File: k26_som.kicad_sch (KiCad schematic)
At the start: 48 parts, among them J6 22-23-2021, M1 XILINX-KRIA-K26, Q6 PJA3441, Q7 DTC014TEBTL

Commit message: Add decoupling to cammera and DP connector, schematic cleanup
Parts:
- added R?: R_0R_0402, antmicro-footprints:0402-res, symbol antmicroResistors0402:R_0R_0402
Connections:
- net GND: now also R?.1
- net VCC_BATT: now also R?.2
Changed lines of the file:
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@@
   (junction (at 85.09 55.88) (diameter 0) (color 0 0 0 0)
   )
-  (junction (at 373.38 177.8) (diameter 0) (color 0 0 0 0)
-  )
-  (junction (at 373.38 175.26) (diameter 0) (color 0 0 0 0)
-  )
   (junction (at 302.006 226.568) (diameter 0) (color 0 0 0 0)
   )
@@
     (stroke (width 0) (type default) (color 0 0 0 0))
   )
+  (wire (pts (xy 19.685 25.4) (xy 19.685 26.67))
+    (stroke (width 0) (type default) (color 0 0 0 0))
+  )
   (bus (pts (xy 196.85 129.54) (xy 196.85 134.62))
     (stroke (width 0) (type default) (color 0 0 0 0))
@@
     (stroke (width 0) (type default) (color 0 0 0 0))
   )
+  (wire (pts (xy 373.38 177.8) (xy 404.495 177.8))
+    (stroke (width 0) (type default) (color 0 0 0 0))
+  )
   (wire (pts (xy 277.368 223.52) (xy 277.368 226.06))
     (stroke (width 0) (type default) (color 0 0 0 0))
@@
     (stroke (width 0) (type default) (color 0 0 0 0))
   )
-  (wire (pts (xy 373.38 177.8) (xy 373.126 177.8))
-    (stroke (width 0) (type default) (color 0 0 0 0))
-  )
   (polyline (pts (xy 344.805 246.38) (xy 344.805 181.61))
     (stroke (width 0) (type default) (color 0 0 0 0))
@@
     (stroke (width 0) (type default) (color 0 0 0 0))
   )
+  (wire (pts (xy 19.685 34.29) (xy 19.685 35.56))
+    (stroke (width 0) (type default) (color 0 0 0 0))
+  )
   (wire (pts (xy 147.32 83.82) (xy 130.81 83.82))
     (stroke (width 0) (type default) (color 0 0 0 0))
@@
     (stroke (width 0) (type default) (color 0 0 0 0))
   )
-  (wire (pts (xy 50.8 25.4) (xy 25.4 25.4))
+  (wire (pts (xy 19.685 25.4) (xy 50.8 25.4))
     (stroke (width 0) (type default) (color 0 0 0 0))
   )
@@
     (stroke (width 0) (type default) (color 0 0 0 0))
   )
+  (wire (pts (xy 373.38 175.26) (xy 404.495 175.26))
+    (stroke (width 0) (type default) (color 0 0 0 0))
+  )
   (wire (pts (xy 81.28 66.04) (xy 96.774 66.04))
     (stroke (width 0) (type default) (color 0 0 0 0))
@@
     (stroke (width 0) (type default) (color 0 0 0 0))
   )
-  (wire (pts (xy 373.38 177.8) (xy 404.114 177.8))
-    (stroke (width 0) (type default) (color 0 0 0 0))
-  )
   (wire (pts (xy 133.35 265.684) (xy 157.48 265.684))
     (stroke (width 0) (type default) (color 0 0 0 0))
@@
     (stroke (width 0) (type default) (color 0 0 0 0))
   )
-  (wire (pts (xy 373.38 175.26) (xy 404.114 175.26))
-    (stroke (width 0) (type default) (color 0 0 0 0))
-  )
   (wire (pts (xy 246.38 86.36) (xy 224.282 86.36))
     (stroke (width 0) (type default) (color 0 0 0 0))
@@
     (stroke (width 0) (type default) (color 0 0 0 0))
   )
-  (wire (pts (xy 373.38 175.26) (xy 373.126 175.26))
-    (stroke (width 0) (type default) (color 0 0 0 0))
-  )
   (wire (pts (xy 317.5 33.02) (xy 342.9 33.02))
     (stroke (width 0) (type default) (color 0 0 0 0))
@@
     (effects (font (size 1.27 1.27)) (justify left bottom))
   )
-  (label "VCCO_HDC_1" (at 404.114 175.26 180)
+  (label "VCCO_HDC_1" (at 404.495 175.26 180)
     (effects (font (size 1.27 1.27)) (justify right bottom))
   )
@@
     (effects (font (size 1.27 1.27)) (justify left bottom))
   )
-  (label "VCCO_HDC_2" (at 404.114 177.8 180)
+  (label "VCCO_HDC_2" (at 404.495 177.8 180)
     (effects (font (size 1.27 1.27)) (justify right bottom))
   )
@@
     (pin "1")
   )
+  (symbol (lib_id "kria-k26-devboard:GND") (at 19.685 35.56 0) (unit 1)
+    (in_bom yes) (on_board yes)
+    (property "Reference" "#PWR?" (id 0) (at 19.685 41.91 0)
+      (effects (font (size 1.27 1.27)) hide)
+    )
+    (property "Value" "GND" (id 1) (at 19.812 39.9542 0))
+    (property "Footprint" "" (id 2) (at 19.685 35.56 0)
+      (effects (font (size 1.27 1.27)) hide)
+    )
+    (property "Datasheet" "" (id 3) (at 19.685 35.56 0)
+      (effects (font (size 1.27 1.27)) hide)
+    )
+    (pin "1")
+  )
   (symbol (lib_id "kria-k26-devboard:C_100n_0402") (at 258.445 272.415 0) (unit 1)
     (in_bom yes) (on_board yes)
@@
     (pin "1")
   )
+  (symbol (lib_id "antmicroResistors0402:R_0R_0402") (at 19.685 30.48 90) (unit 1)
+    (in_bom yes) (on_board yes) (fields_autoplaced)
+    (property "Reference" "R?" (id 0) (at 21.463 29.6454 90)
+      (effects (font (size 1.524 1.524)) (justify right))
+    )
+    (property "Value" "R_0R_0402" (id 1) (at 23.495 30.48 0)
+      (effects (font (size 1.524 1.524)) hide)
+    )
+    (property "Footprint" "antmicro-footprints:0402-res" (id 2) (at 14.605 25.4 0)
+      (effects (font (size 1.524 1.524)) (justify left) hide)
+    )
+    (property "Datasheet" "" (id 3) (at 19.685 30.48 0)
+      (effects (font (size 1.27 1.27)) hide)
+    )
+    (property "Manufacturer" "PANASONIC" (id 4) (at 9.525 25.4 0)
+      (effects (font (size 1.524 1.524)) (justify left) hide)
+    )
+    (property "MPN" "ERJ2GE0R00X" (id 5) (at 12.065 25.4 0)
+      (effects (font (size 1.524 1.524)) (justify left) hide)
+    )
+    (property "Val" "0R" (id 6) (at 21.463 32.4105 90)
+      (effects (font (size 1.27 1.27)) (justify right))
+    )
+    (pin "1")
+    (pin "2")
+  )
   (symbol (lib_id "kria-k26-devboard:TP_SMD_0_75MM") (at 386.715 206.375 90) (mirror x) (unit 1)

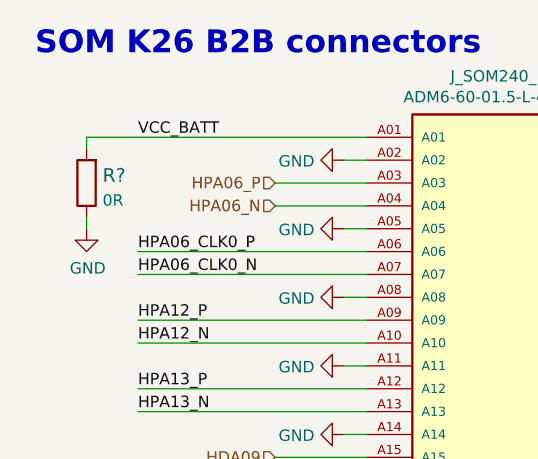
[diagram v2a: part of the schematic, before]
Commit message: Finish implementing review changes on schematic. Push to PCB
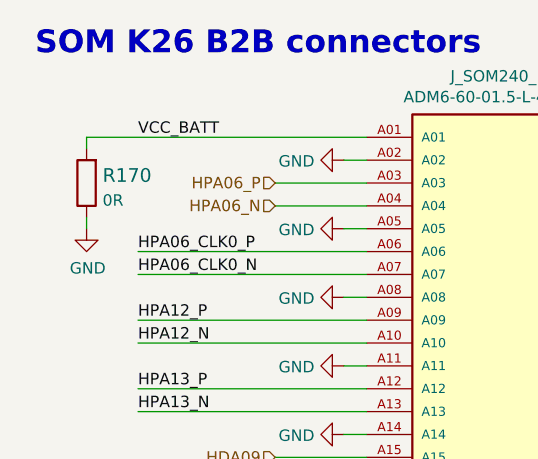
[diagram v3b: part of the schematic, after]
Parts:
- gave numbers to parts that had none: 1
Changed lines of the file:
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@@
   (title_block
     (title "Kria K26 Devboard")
-    (date "2023-02-15")
+    (date "2023-03-03")
     (rev "1.1.1")
     (company "Antmicro")
@@
   (symbol (lib_id "antmicroResistors0402:R_0R_0402") (at 19.685 30.48 90) (unit 1)
     (in_bom yes) (on_board yes) (fields_autoplaced)
-    (property "Reference" "R?" (id 0) (at 21.463 29.6454 90)
+    (property "Reference" "R170" (id 0) (at 21.463 29.6454 90)
       (effects (font (size 1.524 1.524)) (justify right))
     )

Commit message: Loclib of the project
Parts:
- R170: footprint antmicro-footprints:0402-res -> kria-k26-devboard-footprints:0402-res; symbol antmicroResistors0402:R_0R_0402 -> kria-k26-devboard:R_0R_0402

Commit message: Bom optimization
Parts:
- removed C126: C_1u_1210_100V, kria-k26-devboard-footprints:1210-cap, symbol kria-k26-devboard:C_1u_1210_100V
- added C126, C250, C251, C252, C253: C_100n_0402, kria-k26-devboard-footprints:0402-cap, symbol kria-k26-devboard:C_100n_0402
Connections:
- net GND: now also C126.2, C250.2, C251.2, C252.2, C253.2
- net at D3.K, FB1.1, Q6.3 (D): now also C126.1, C250.1, C251.1, C252.1, C253.1
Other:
- moved on the sheet: D3, FB1, FB2, J6

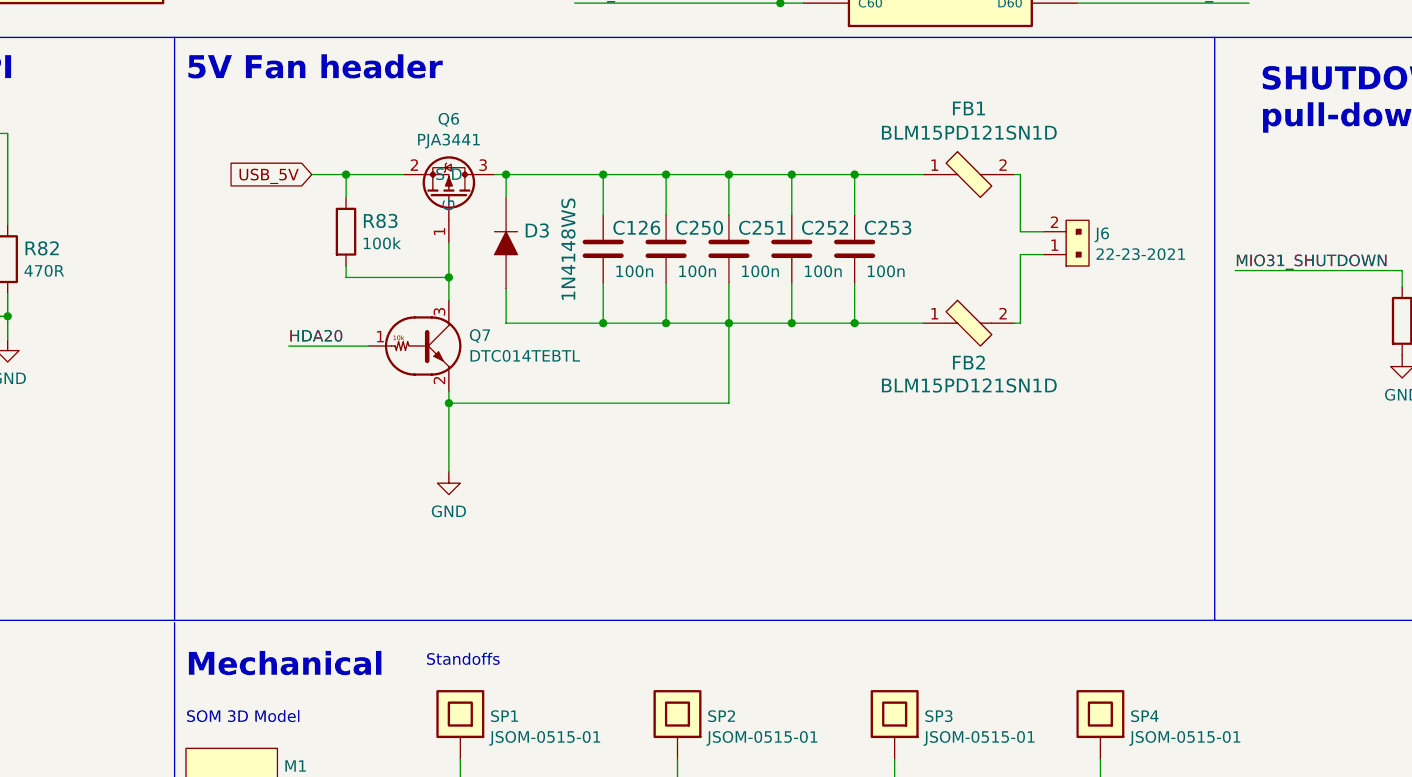
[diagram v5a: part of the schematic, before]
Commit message: Fix fan logic inversion
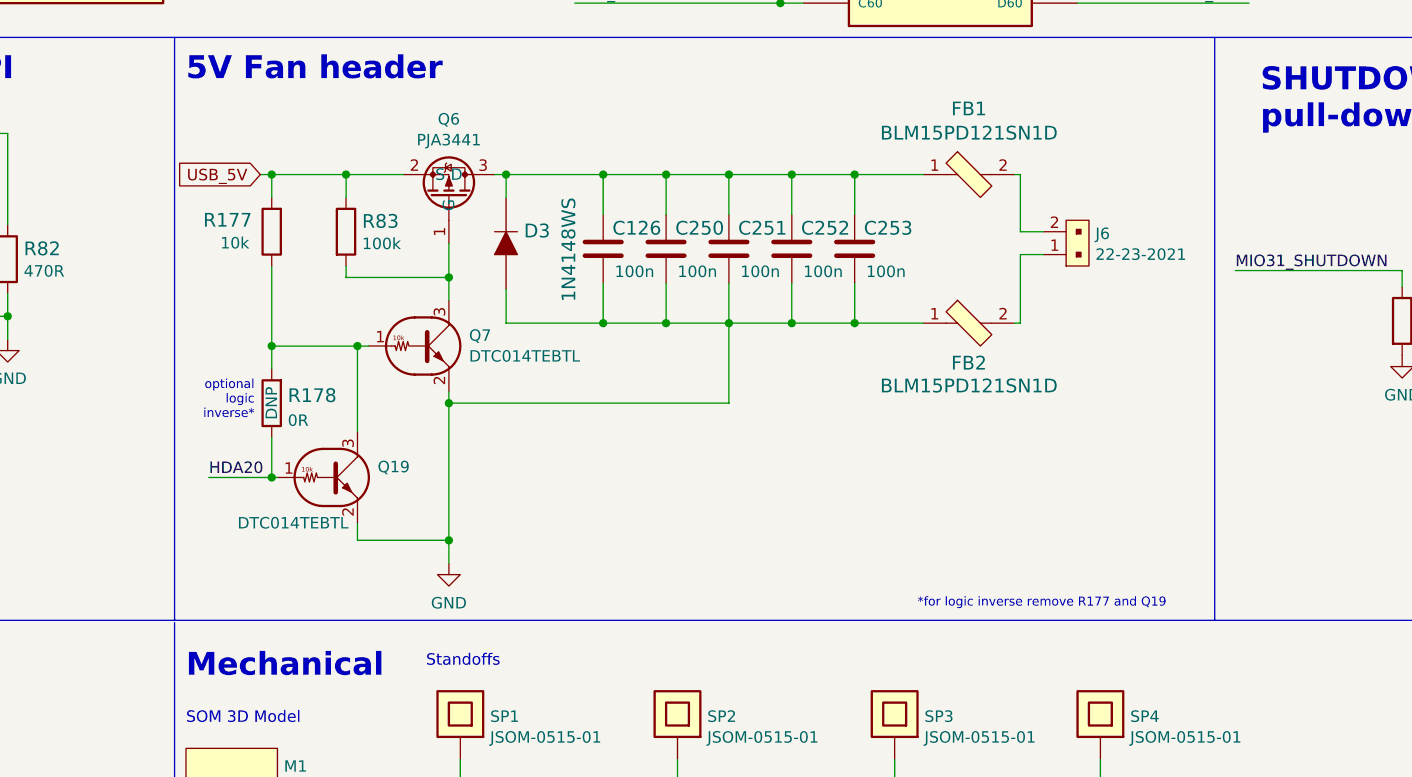
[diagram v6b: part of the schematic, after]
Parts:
- added Q19: DTC014TEBTL, kria-k26-devboard-footprints:SOT-416, symbol kria-k26-devboard:DTC014TEBTL
- added R177: R_10k_0402, antmicro-footprints:0402-res, symbol antmicroResistors0402:R_10k_0402
- added R178: R_0R_0402, antmicro-footprints:0402-res, symbol antmicroResistors0402:R_0R_0402
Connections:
- net GND: now also Q19.2 (E)
- net HDA20: now also Q19.1 (B), R178.1; no longer Q7.1 (B)
- net USB_5V: now also R177.2
- new net: Q19.3 (C), Q7.1 (B), R177.1, R178.2
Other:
- note added: "*for logic inverse remove R177 and Q19"
- note added: "optional logic inverse*"
